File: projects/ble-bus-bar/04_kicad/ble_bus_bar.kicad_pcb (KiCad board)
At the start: 2 copper layers, 165 x 64 mm, 101 parts, among them J1 PORT 1 M4 LUG, J10 DEBUG UART DNP, J2 PORT 2 M4 LUG, J3 PORT 3 M4 LUG, J4 PORT 4 M4 LUG, J5 PORT 5 M4 LUG, J6 PORT 6 M4 LUG, J7 +12-24V IN M5 LUG, J8 GND REF M4 LUG, J9 TYPE-C-31-M-12, SW1 RESET, SW2 BOOT, U1 INA238AIDGSR, U10 USBLC6-2SC6, U11 W25Q64JVSSIQ, U2 INA238AIDGSR, U3 INA238AIDGSR, U4 INA238AIDGSR, U5 INA238AIDGSR, U6 INA238AIDGSR, U7 ESP32-C3-WROOM-02-N4, U8 LMR16006XDDCR, U9 AMS1117-3.3

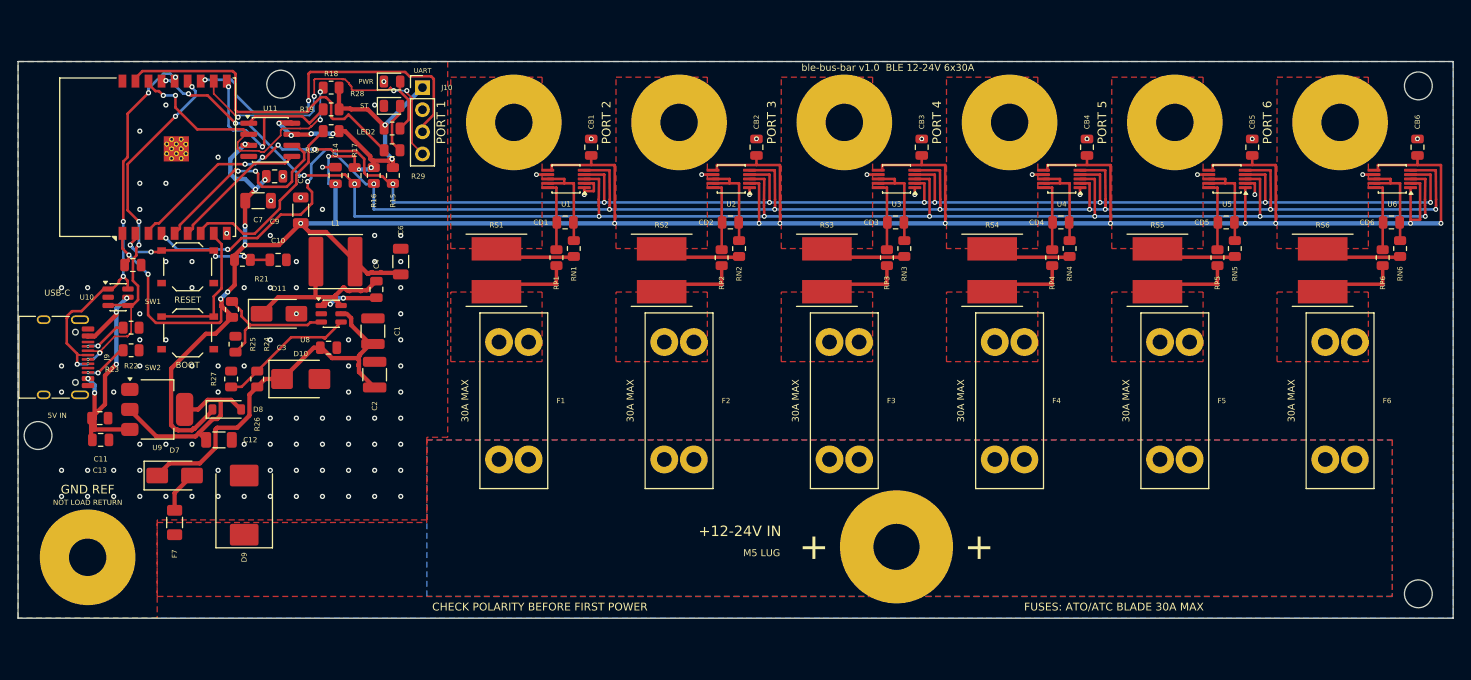
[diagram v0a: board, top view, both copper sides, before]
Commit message: ble-bus-bar: WIP CHECKPOINT (not a gate) — wide-SOIC U11 fix (twin catch), hardest-first wave order, J10/LED/R-col relocation; board at 1 violation + 4 unconnected mid-cleanup
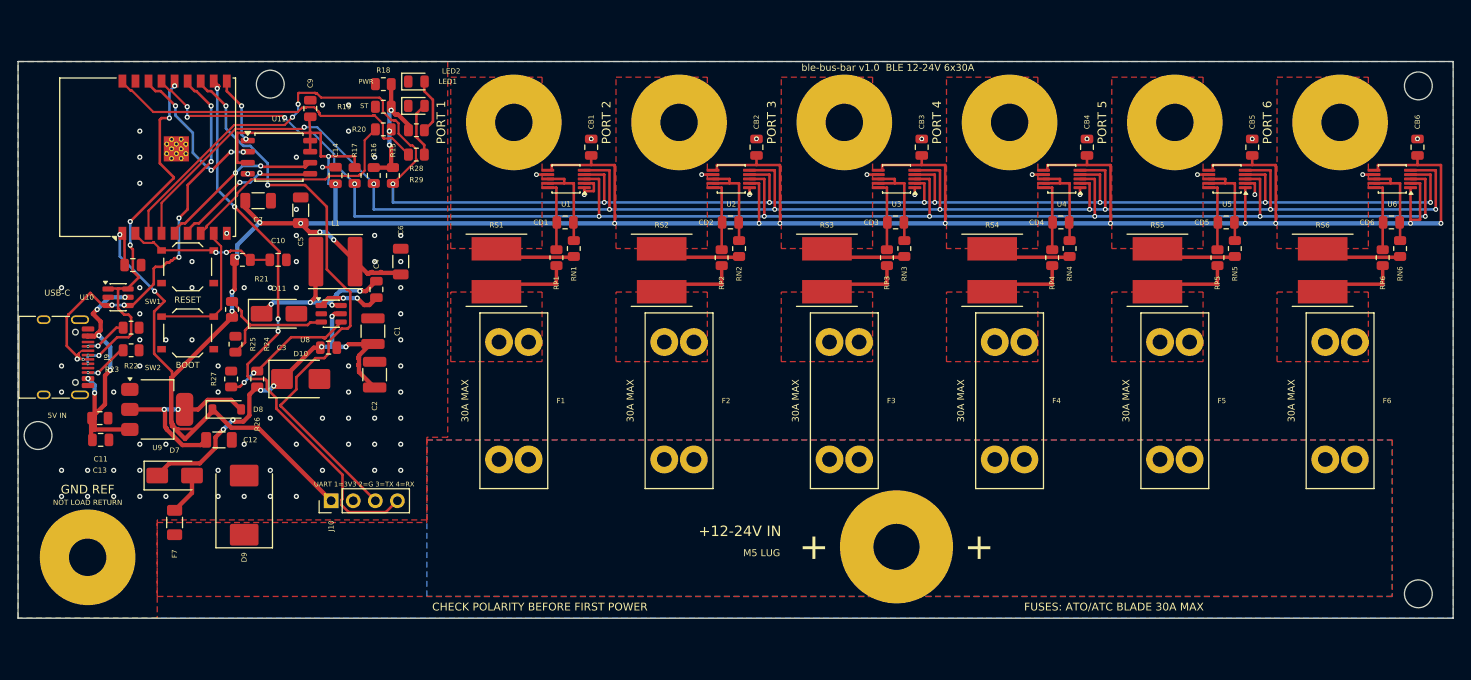
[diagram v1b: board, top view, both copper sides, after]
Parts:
- U11: footprint Package_SO:SOIC-8_3.9x4.9mm_P1.27mm -> Package_SO:SOIC-8_5.3x5.3mm_P1.27mm
- moved J10 48.6 mm to (86.0, 100.5), turned to 90 degrees
- moved C9 8.81 mm to (83.6, 55.4), turned to 90 degrees
- moved R18 6.01 mm to (92.0, 52.6)
- moved R19 6.01 mm to (92.0, 55.2)
- moved R20 6.00 mm to (92.0, 57.8)
- moved R29 2.84 mm to (95.8, 60.7)
- moved R28 2.81 mm to (95.8, 57.9)
- moved LED1 2.80 mm to (95.8, 52.3)
- moved LED2 2.80 mm to (95.8, 55.1)
- moved U11 2.24 mm to (80.0, 61.0)
- moved H4 1.20 mm to (79.0, 52.6)
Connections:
- U7 pad 17: LED_ST -> unconnected-(U7-IO1/LED-Pad17)
- U7 pad 18: unconnected-(U7-IO0-Pad18) -> LED_ST
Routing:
- net RXD: track 38.3 -> 66.8 mm
- net TXD: track 40.6 -> 68.0 mm
- net FLASH_CS: track 23.9 -> 8.04 mm
- net SDA: track 193.1 -> 208.3 mm, vias 12 -> 10
- net SPI_MISO: track 34.2 -> 19.4 mm
- net 3V3: track 399.5 -> 410.1 mm, vias 29 -> 23
- net USB_DM: track 45.4 -> 51.0 mm, vias 6 -> 8
- net IO8: track 22.7 -> 27.8 mm
- net SPI_CLK: track 24.6 -> 19.5 mm
- net ALERT: track 190.2 -> 192.1 mm, vias 11 -> 10
- net VIN_E: track 44.6 -> 46.2 mm, vias 0 -> 7
- net SPI_MOSI: track 16.1 -> 17.6 mm, vias 0 -> 2
- net LED_ST: track 38.5 -> 39.8 mm
- net VLDO: track 23.5 -> 22.2 mm, vias 0 -> 2
- net USB_DP: track 46.5 -> 45.4 mm, vias 6 -> 7
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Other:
- board text added: "UART 1=3V3 2=G 3=TX 4=RX"
- board text removed: "UART"

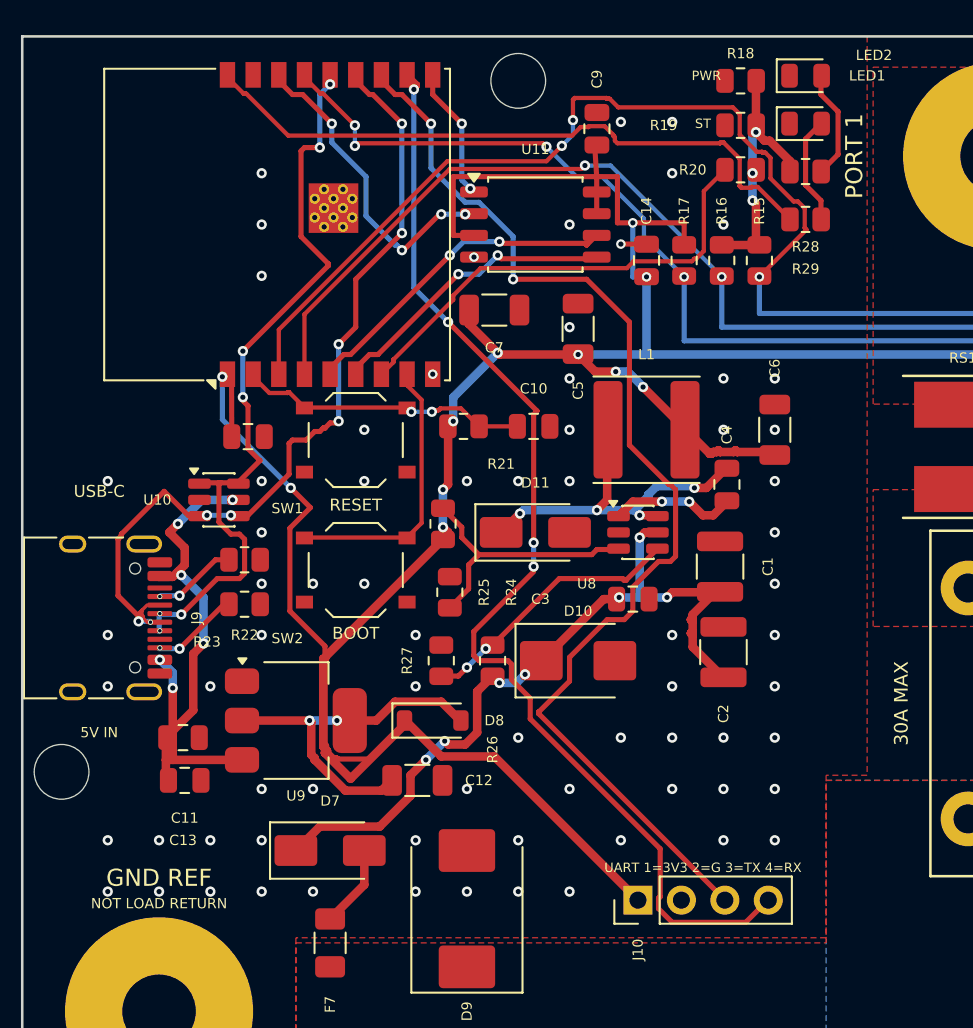
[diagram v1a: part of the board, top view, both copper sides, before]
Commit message: ble-bus-bar: BOARD GATE GREEN (post-rework) — DRC severity-all 0/0/0, ERC 0, audit PASS. Rework: U11 wide-SOIC (twin catch), hardest-first KRT waves, deterministic flash-power/C8/corridor-bridge hand links, junction-via healer; chain promoted 03_src/route/r3
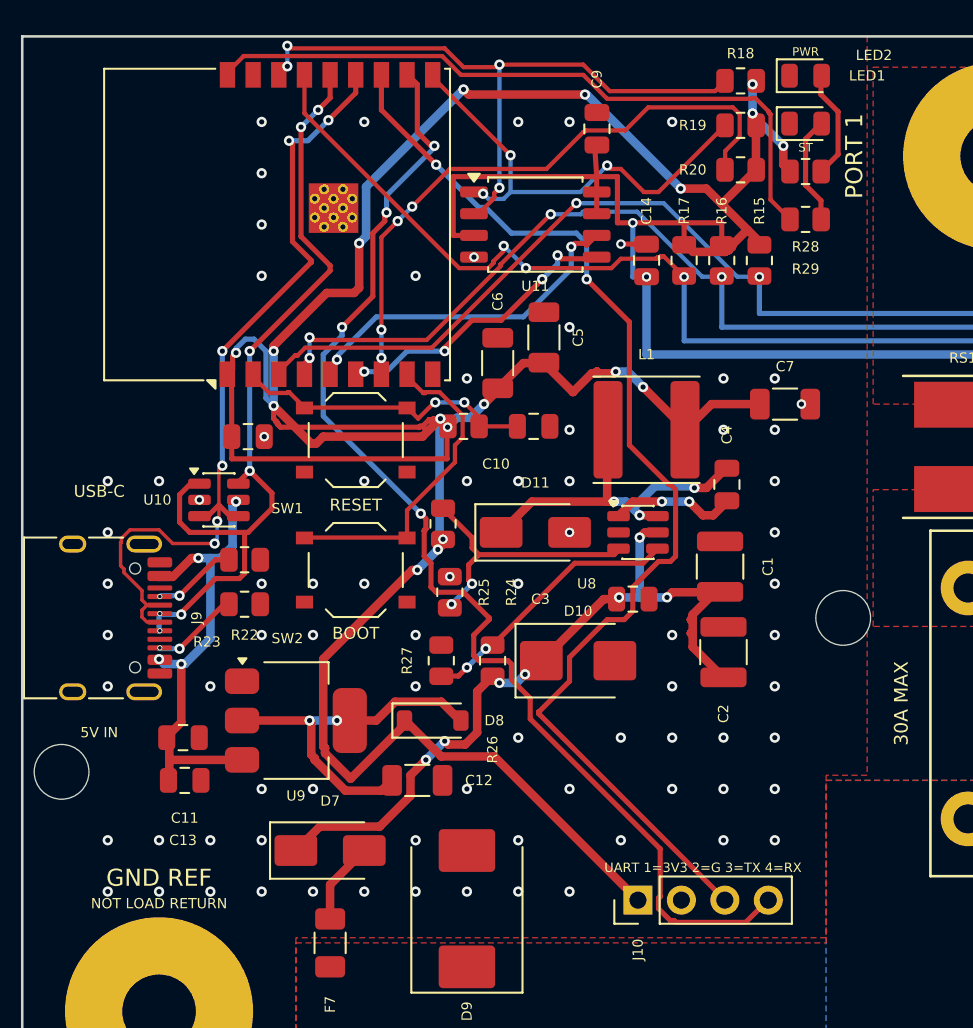
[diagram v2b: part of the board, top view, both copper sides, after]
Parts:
- moved H4 36.7 mm to (98.0, 84.0)
- moved C7 17.9 mm to (94.6, 71.5)
- moved C6 16.7 mm to (77.8, 69.1)
- moved C5 2.06 mm to (80.5, 67.6)
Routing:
- net 3V3: track 410.1 -> 466.1 mm, vias 23 -> 29
- net SPI_MISO: track 19.4 -> 38.9 mm
- net FLASH_CS: track 8.04 -> 26.8 mm, vias 2 -> 3
- net SDA: track 208.3 -> 192.3 mm, vias 10 -> 9
- net IO8: track 27.8 -> 36.2 mm, vias 0 -> 4
- net VUSB: track 36.7 -> 28.6 mm, vias 6 -> 4
- net RXD: track 66.8 -> 71.5 mm
- net USB_DP: track 45.4 -> 49.5 mm
- net USB_DM: track 51.0 -> 47.6 mm, vias 8 -> 6
- net BOOT9: track 16.3 -> 19.5 mm
- net SCL: track 207.7 -> 204.9 mm, vias 9 -> 11
- net ALERT: track 192.1 -> 193.9 mm, vias 10 -> 9
- net LED_ST: track 39.8 -> 41.2 mm
- net SPI_CLK: track 19.5 -> 20.6 mm
- net TXD: track 68.0 -> 67.3 mm
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
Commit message: ble-bus-bar v1.1: durable anchoring GATE GREEN — 7x M4 plated mounts (ADR-0007, A4/D9), board 165x74, DRC 0/0/0, audit PASS (new IM mount checks)
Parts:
- added H5: Mount_M4, bbar:Mount_M4_Plated, F.Cu at (163.0, 114.1)
- added H6: Mount_M4, bbar:Mount_M4_Plated, F.Cu at (193.0, 114.1)
- added H7: Mount_M4, bbar:Mount_M4_Plated, F.Cu at (69.5, 114.1)
- H1, H2, H3, H4: value MountingHole_3.2mm_M3 -> Mount_M4; footprint MountingHole_3.2mm_M3 -> bbar:Mount_M4_Plated
- moved H1 77.7 mm to (117.0, 49.9)
- moved H3 63.9 mm to (193.0, 49.9)
- moved H2 56.1 mm to (155.0, 49.9)
- moved H4 35.6 mm to (117.0, 114.1)
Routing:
- net GND: vias 97 -> 101
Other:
- board size 165 x 64 mm -> 165 x 74 mm
- board text added: "BEFORE FIRST POWER"
- board text added: "CHECK POLARITY"
- board text added: "H5"
- board text added: "H6"
- board text added: "H7"
- board text added: "ble-bus-bar v1.1 BLE 12-24V 6x30A"
- board text removed: "CHECK POLARITY BEFORE FIRST POWER"
- board text removed: "ble-bus-bar v1.0 BLE 12-24V 6x30A"
